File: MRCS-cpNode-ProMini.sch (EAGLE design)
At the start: 55 parts, among them CON1 0.100, CON2 0.100, CON3 0.100, CON4 0.100, J1 0.100, J2 0.100, J3 2.1mm, P1 CA CC, U1 MAX3465CPD, U2 NE555P

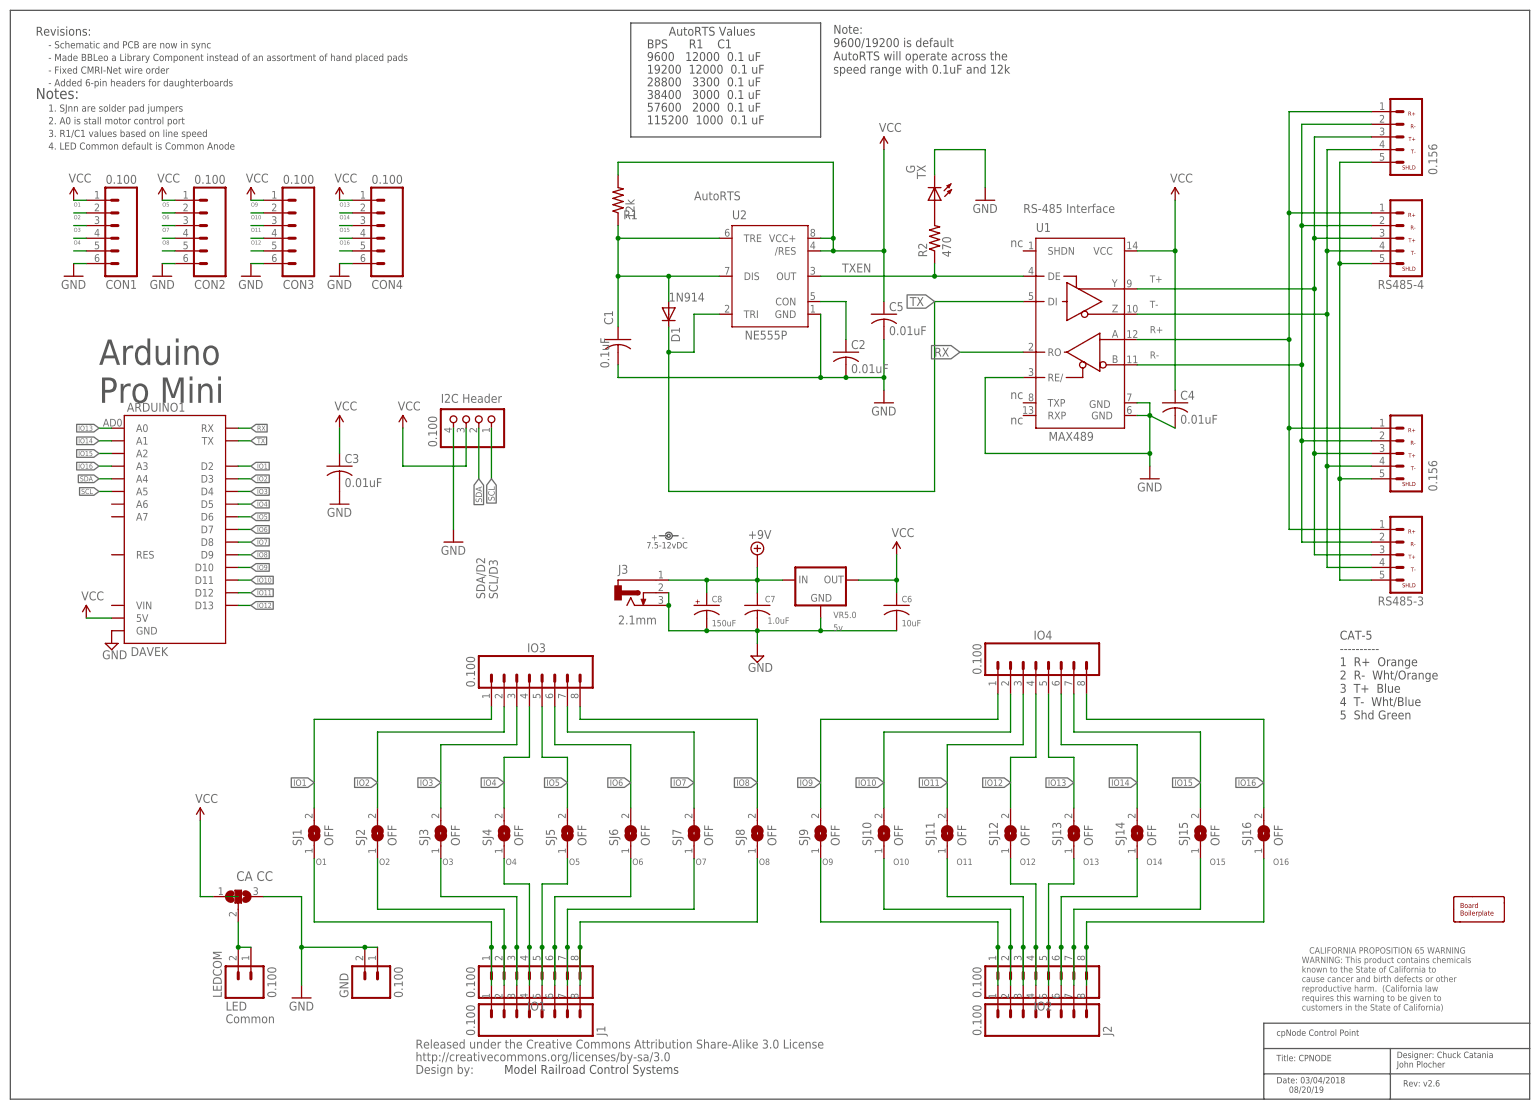
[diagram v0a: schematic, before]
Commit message: add pullup to pin13
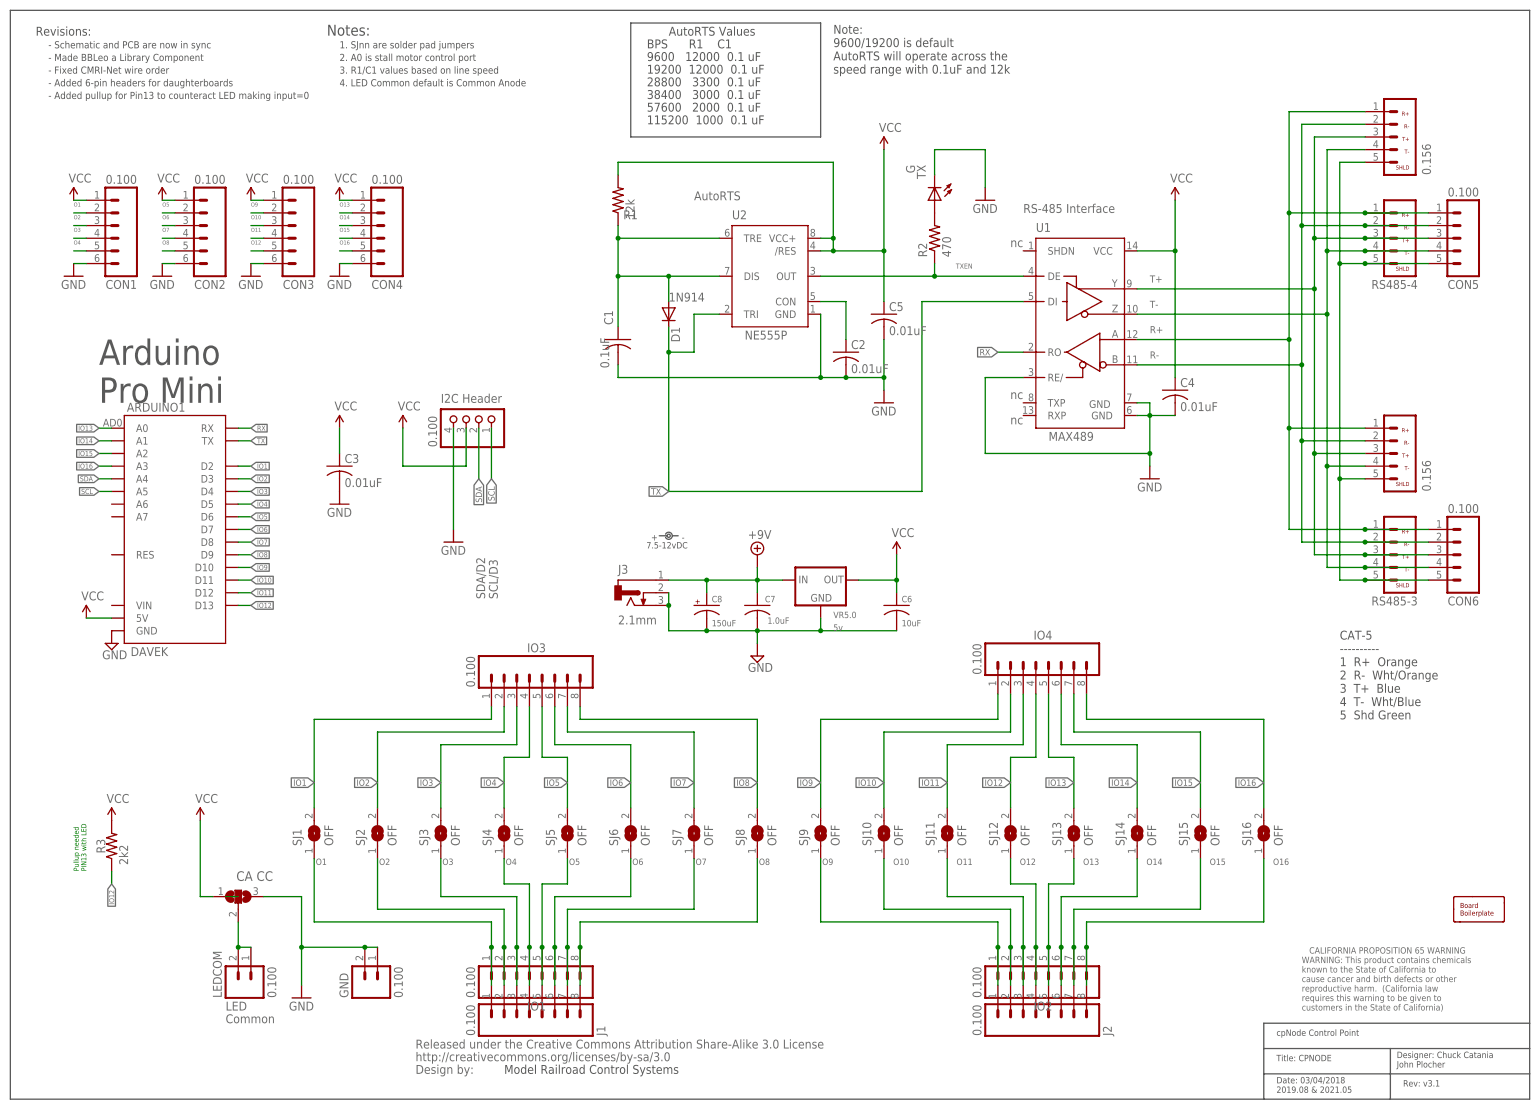
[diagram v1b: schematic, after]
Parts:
- added CON5, CON6: 0.100, SPCoast:CONNECTOR-M05LOCK
- added R3: 2k2, SPCoast:RPTH04
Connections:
- net N$54 renamed TXEN
- net IO12: now also R3.1
- net R+: now also CON5.1, CON6.1
- net R-: now also CON5.2, CON6.2
- net SHIELD: now also CON5.5, CON6.5
- net T+: now also CON5.3, CON6.3
- net T-: now also CON5.4, CON6.4
- net VCC: now also R3.2
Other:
- note added: "- Added pullup for Pin13 to counteract LED making input=0"
- note added: "- Made BBLeo a Library Component"
- note added: "Date: 03/04/2018 2019.08 & 2021.05"
- note added: "Pullup needed PIN13 with LED"
- note added: "Rev: v3.1"
- note removed: "- Made BBLeo a Library Component instead of an assortment of hand placed pads"
- note removed: "Date: 03/04/2018 08/20/19"
- note removed: "Rev: v2.6"
- note removed: "TXEN"
- moved on the sheet: C4, RS485-3, RS485-4
